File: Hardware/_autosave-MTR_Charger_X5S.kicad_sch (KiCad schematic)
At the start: 65 parts, among them J1 Korean Hroparts Elec TYPE-C-3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, J2 Micro_SD_Card, Q1 IRF7324TRPBF, SW1 Boot, SW2 Reset, U1 W25Q16JVUXIQ, U2 RP2040, U3 ADS7830IPWR, U4 ADS7830IPWR, U5 ESDA25W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

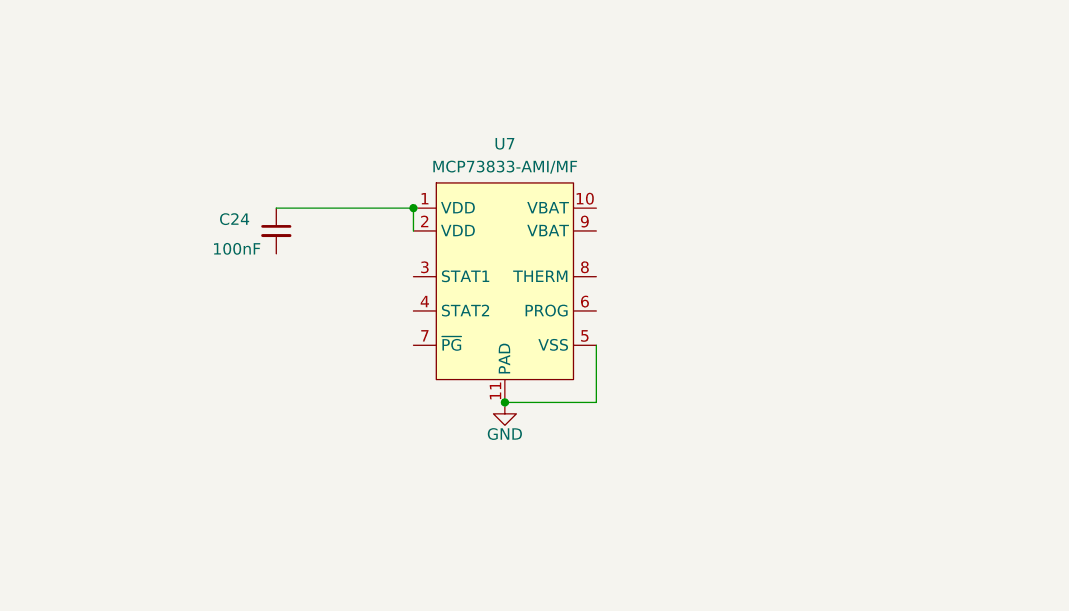
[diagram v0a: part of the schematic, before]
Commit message: Current and Voltage sensing done
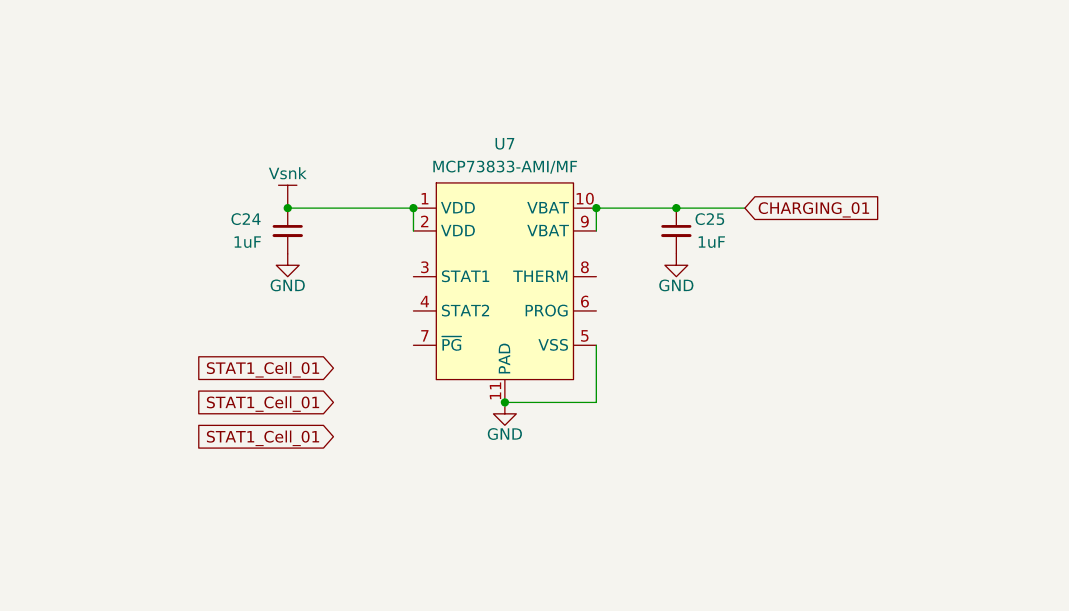
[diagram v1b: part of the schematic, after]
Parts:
- added C25: 1uF, Capacitor_SMD:C_1206_3216Metric, symbol Device:C_Small
- C24: value 100nF -> 1uF
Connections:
- net GND: now also C24.2, C25.2
- net Vsnk: now also C24.1, U7.1 (VDD), U7.2 (VDD)
- net CHARGING_01: now reaches U7.10 (VBAT)
- net CHARGING_01: now also U7.9 (VBAT), C25.1
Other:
- moved on the sheet: C24
